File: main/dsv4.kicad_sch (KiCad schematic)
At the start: 3 parts, among them J101 Conn_01x02, J102 Conn_01x02, J103 Conn_01x02

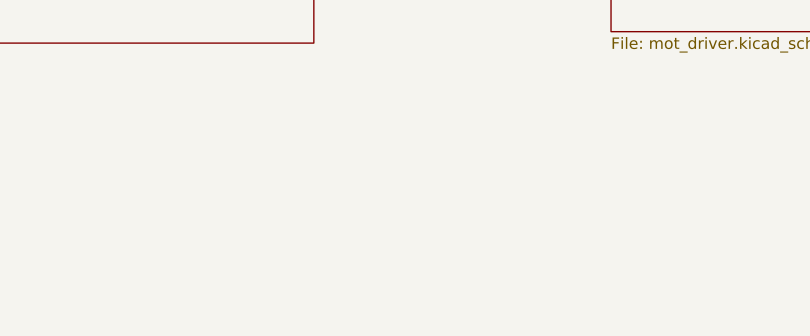
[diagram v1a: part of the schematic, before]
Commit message: Start re-doing routing
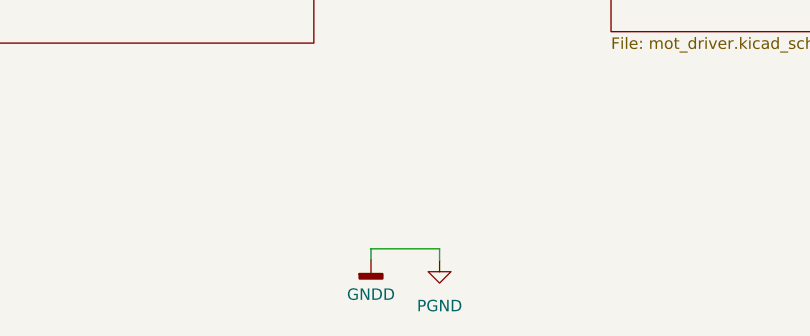
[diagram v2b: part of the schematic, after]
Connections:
- net PGND renamed GNDD
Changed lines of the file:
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@@
+	(wire
+		(pts
+			(xy 110.49 156.21) (xy 110.49 157.48)
+		)
+		(stroke
+			(width 0)
+			(type default)
+		)
+	)
 	(wire
 		(pts
@@
 	(wire
 		(pts
+			(xy 118.11 157.48) (xy 118.11 156.21)
+		)
+		(stroke
+			(width 0)
+			(type default)
+		)
+	)
+	(wire
+		(pts
 			(xy 259.08 119.38) (xy 262.89 119.38)
 		)
@@
 		(pts
 			(xy 104.14 106.68) (xy 123.19 106.68)
+		)
+		(stroke
+			(width 0)
+			(type default)
+		)
+	)
+	(wire
+		(pts
+			(xy 118.11 156.21) (xy 110.49 156.21)
 		)
 		(stroke
@@
 				(path "/c07e9297-fde8-4755-803e-d05072cd6096"
 					(reference "#PWR0101")
+					(unit 1)
+				)
+			)
+		)
+	)
+	(symbol
+		(lib_name "GND_1")
+		(lib_id "power:GND")
+		(at 118.11 157.48 0)
+		(unit 1)
+		(exclude_from_sim no)
+		(in_bom yes)
+		(on_board yes)
+		(dnp no)
+		(fields_autoplaced yes)
+		(property "Reference" "#PWR0107"
+			(at 118.11 163.83 0)
+			(effects
+				(font
+					(size 1.27 1.27)
+				)
+				(hide yes)
+			)
+		)
+		(property "Value" "PGND"
+			(at 118.11 162.56 0)
+			(effects
+				(font
+					(size 1.27 1.27)
+				)
+			)
+		)
+		(property "Footprint" ""
+			(at 118.11 157.48 0)
+			(effects
+				(font
+					(size 1.27 1.27)
+				)
+				(hide yes)
+			)
+		)
+		(property "Datasheet" ""
+			(at 118.11 157.48 0)
+			(effects
+				(font
+					(size 1.27 1.27)
+				)
+				(hide yes)
+			)
+		)
+		(property "Description" "Power symbol creates a global label with name \"GND\" , ground"
+			(at 118.11 157.48 0)
+			(effects
+				(font
+					(size 1.27 1.27)
+				)
+				(hide yes)
+			)
+		)
+		(pin "1"
+		)
+		(instances
+			(project "dsv4"
+				(path "/c07e9297-fde8-4755-803e-d05072cd6096"
+					(reference "#PWR0107")
 					(unit 1)
 				)
@@
 					(unit 1)
 				)
+			)
+		)
+	)
+	(symbol
+		(lib_id "power:GNDD")
+		(at 110.49 157.48 0)
+		(unit 1)
+		(exclude_from_sim no)
+		(in_bom yes)
+		(on_board yes)
+		(dnp no)
+		(fields_autoplaced yes)
+		(property "Reference" "#PWR0106"
+			(at 110.49 163.83 0)
+			(effects
+				(font
+					(size 1.27 1.27)
+				)
+				(hide yes)
+			)
+		)
+		(property "Value" "GNDD"
+			(at 110.49 161.29 0)
+			(effects
+				(font
+					(size 1.27 1.27)
+				)
+			)
+		)
+		(property "Footprint" ""
+			(at 110.49 157.48 0)
+			(effects
+				(font
+					(size 1.27 1.27)
+				)
+				(hide yes)
+			)
+		)
+		(property "Datasheet" ""
+			(at 110.49 157.48 0)
+			(effects
+				(font
+					(size 1.27 1.27)
+				)
+				(hide yes)
+			)
+		)
+		(property "Description" "Power symbol creates a global label with name \"GNDD\" , digital ground"
+			(at 110.49 157.48 0)
+			(effects
+				(font
+					(size 1.27 1.27)
+				)
+				(hide yes)
+			)
+		)
+		(pin "1"
+		)
+		(instances
+			(project "dsv4"
+				(path "/c07e9297-fde8-4755-803e-d05072cd6096"
+					(reference "#PWR0106")
+					(unit 1)
+				)
